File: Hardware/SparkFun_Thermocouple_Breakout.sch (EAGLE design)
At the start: 19 parts, among them U1 MAX31855K

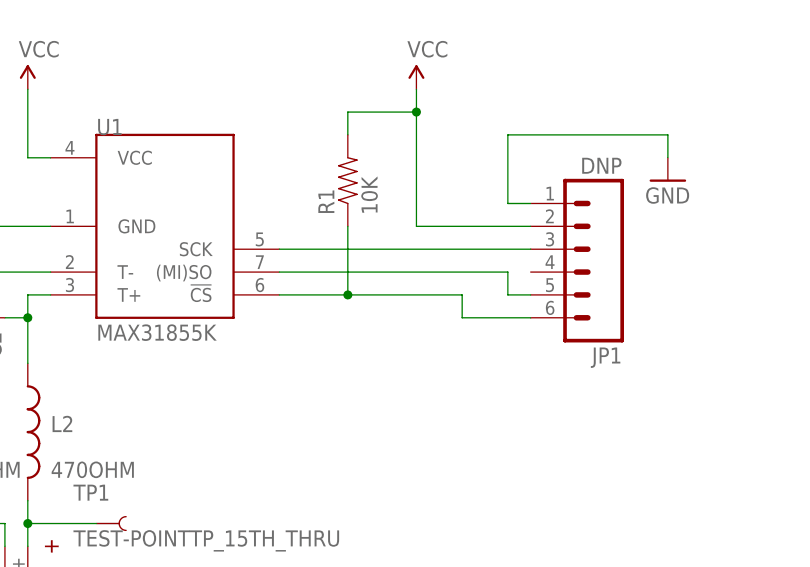
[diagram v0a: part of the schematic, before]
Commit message: Swapped a pin
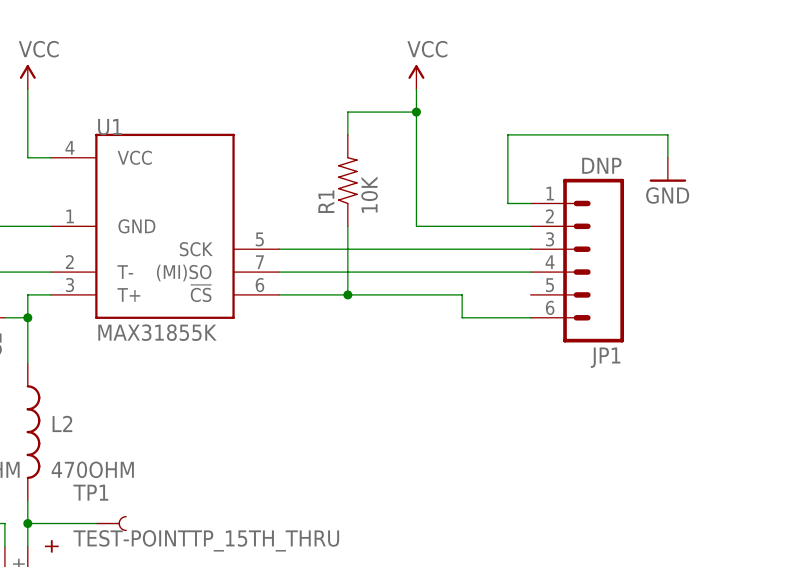
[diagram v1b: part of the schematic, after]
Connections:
- net N$2: now also JP1.4; no longer JP1.5
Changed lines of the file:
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@@
 <segment>
 <pinref part="U1" gate="G$1" pin="(MI)SO"/>
-<wire x1="129.54" y1="93.98" x2="154.94" y2="93.98" width="0.1524" layer="91"/>
-<pinref part="JP1" gate="G$1" pin="5"/>
-<wire x1="157.48" y1="91.44" x2="154.94" y2="91.44" width="0.1524" layer="91"/>
-<wire x1="154.94" y1="91.44" x2="154.94" y2="93.98" width="0.1524" layer="91"/>
+<wire x1="129.54" y1="93.98" x2="157.48" y2="93.98" width="0.1524" layer="91"/>
+<pinref part="JP1" gate="G$1" pin="4"/>
 </segment>
 </net>
